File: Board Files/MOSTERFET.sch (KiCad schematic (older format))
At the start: 27 parts, among them CN11 Jumper_NC_Small, CN21 Jumper_NC_Small, J11 XT-60, J12 XT-60, J21 XT-60, J22 XT-60, Q11 AUIRFSA8409-7P, Q21 AUIRFSA8409-7P, U11 TLP182, U21 TLP182

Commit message: Fixed footprint reference
Fixed footprint Reference for open harware symbole
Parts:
- J11, J21: value XT-60 -> XT-60-M; Manufacturer Number XT-60 -> XT-60-M
- J12, J22: value XT-60 -> XT-60-F; Manufacturer Number XT-60 -> XT-60-F
- LO1: footprint MyLib:OPEN_GEAR -> Symbols:OSHW-Symbol_8.9x8mm_SilkScreen
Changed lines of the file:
@@
 P 4925 3750
 F 0 "J12" H 4875 3600 50  0000 L CNN
-F 1 "XT-60" H 5003 3700 50  0001 L CNN
+F 1 "XT-60-F" H 5003 3700 50  0001 L CNN
 F 2 "MyLib:XT60" H 4925 3750 50  0001 C CNN
 F 3 "" H 4925 3750 50  0001 C CNN
-F 4 "XT-60" H 4925 3750 50  0001 C CNN "Manufacturer Number"
+F 4 "XT-60-F" H 4925 3750 50  0001 C CNN "Manufacturer Number"
 F 5 "SparkFun" H 4925 3750 50  0001 C CNN "Supplier"
 F 6 "PRT-10474" H 4925 3750 50  0001 C CNN "Supplier Part No"
@@
 P 4925 3025
 F 0 "J11" H 4875 2875 50  0000 L CNN
-F 1 "XT-60" H 5003 2975 50  0001 L CNN
+F 1 "XT-60-M" H 5003 2975 50  0001 L CNN
 F 2 "MyLib:XT60" H 4925 3025 50  0001 C CNN
 F 3 "" H 4925 3025 50  0001 C CNN
-F 4 "XT-60" H 4925 3025 50  0001 C CNN "Manufacturer Number"
+F 4 "XT-60-M" H 4925 3025 50  0001 C CNN "Manufacturer Number"
 F 5 "SparkFun" H 4925 3025 50  0001 C CNN "Supplier"
 F 6 "PRT-10474" H 4925 3025 50  0001 C CNN "Supplier Part No"
@@
 P 9025 3825
 F 0 "J22" H 8975 3675 50  0000 L CNN
-F 1 "XT-60" H 9103 3775 50  0001 L CNN
+F 1 "XT-60-F" H 9103 3775 50  0001 L CNN
 F 2 "MyLib:XT60" H 9025 3825 50  0001 C CNN
 F 3 "" H 9025 3825 50  0001 C CNN
-F 4 "XT-60" H 9025 3825 50  0001 C CNN "Manufacturer Number"
+F 4 "XT-60-F" H 9025 3825 50  0001 C CNN "Manufacturer Number"
 F 5 "SparkFun" H 9025 3825 50  0001 C CNN "Supplier"
 F 6 "PRT-10474" H 9025 3825 50  0001 C CNN "Supplier Part No"
@@
 P 9025 3100
 F 0 "J21" H 8975 2950 50  0000 L CNN
-F 1 "XT-60" H 9103 3050 50  0001 L CNN
+F 1 "XT-60-M" H 9103 3050 50  0001 L CNN
 F 2 "MyLib:XT60" H 9025 3100 50  0001 C CNN
 F 3 "" H 9025 3100 50  0001 C CNN
-F 4 "XT-60" H 9025 3100 50  0001 C CNN "Manufacturer Number"
+F 4 "XT-60-M" H 9025 3100 50  0001 C CNN "Manufacturer Number"
 F 5 "SparkFun" H 9025 3100 50  0001 C CNN "Supplier"
 F 6 "PRT-10474" H 9025 3100 50  0001 C CNN "Supplier Part No"
@@
 F 0 "LO1" H 1575 7075 50  0001 C CNN
 F 1 "Logo_Open_Hardware_Large" H 1575 6175 50  0001 C CNN
-F 2 "MyLib:OPEN_GEAR" H 1575 6575 50  0001 C CNN
+F 2 "Symbols:OSHW-Symbol_8.9x8mm_SilkScreen" H 1575 6575 50  0001 C CNN
 F 3 "~" H 1575 6575 50  0001 C CNN
 	1    1575 6575

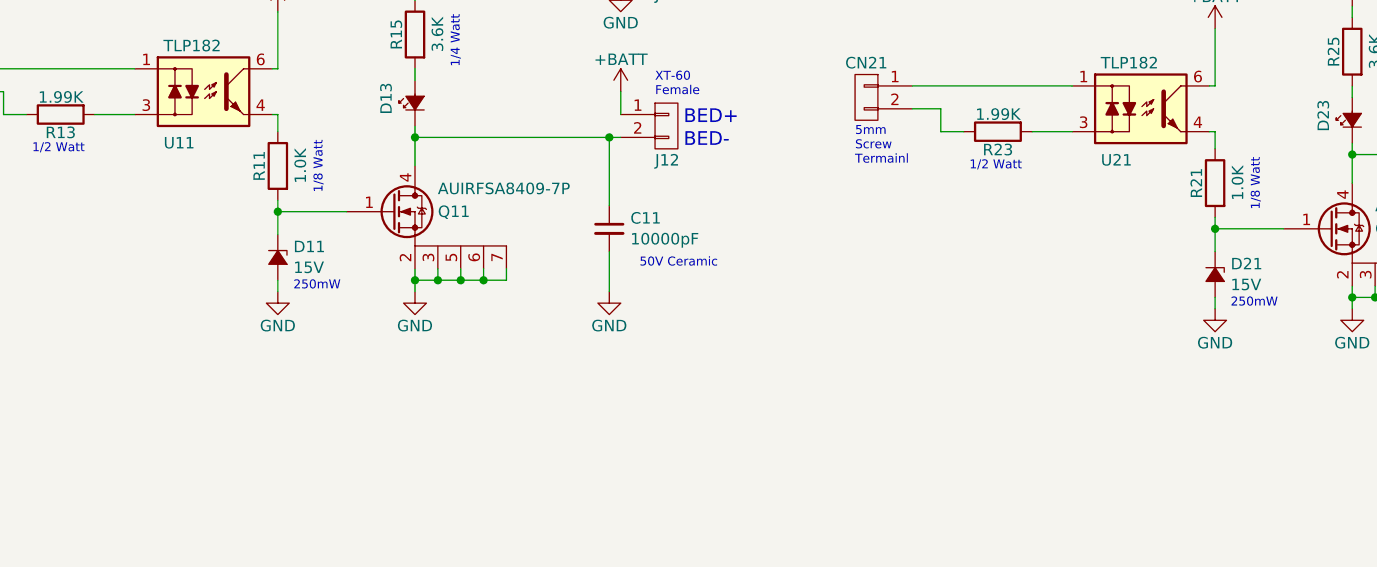
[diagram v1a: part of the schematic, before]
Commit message: Added Bleed resistot
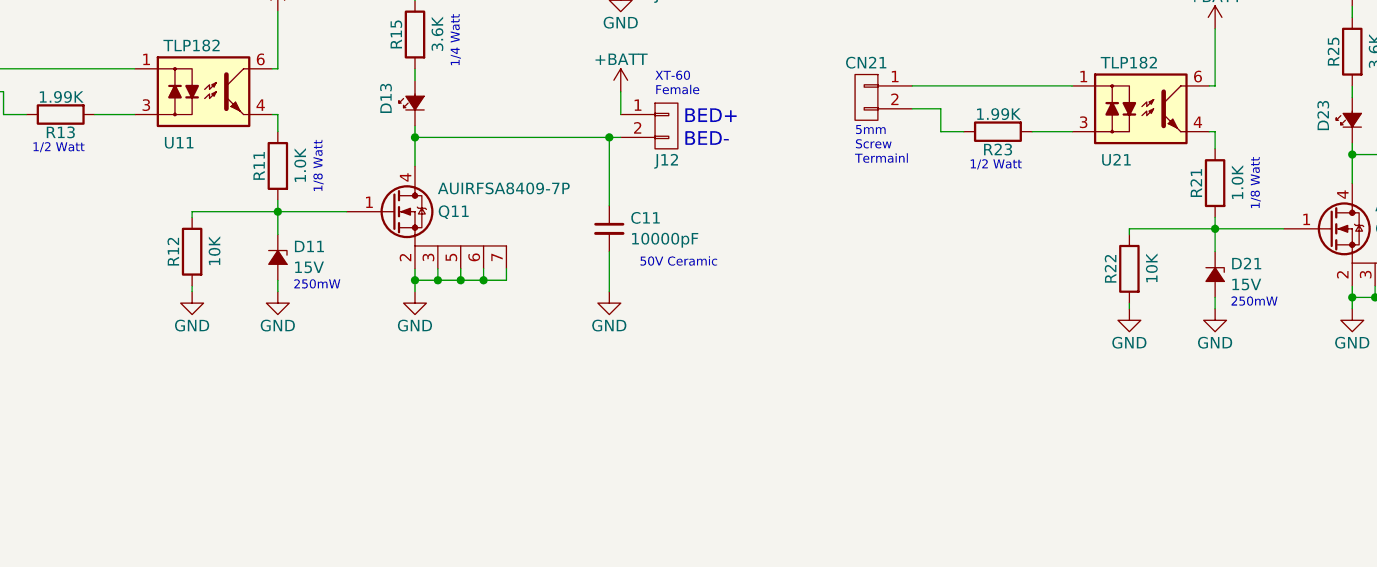
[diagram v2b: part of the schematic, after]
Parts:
- added R12, R22: 10K, Resistors_SMD:R_1206_HandSoldering, symbol Device:R
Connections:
- net GND: now also R12.2, R22.2
- net at D11.3 (K), Q11.1 (G), R11.2: now also R12.1
- net at D21.3 (K), Q21.1 (G), R21.2: now also R22.1
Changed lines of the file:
@@
 Wire Wire Line
 	3825 3800 4675 3800
+$Comp
+L Device:R R12
+U 1 1 5E79AAFD
+P 2850 4300
+F 0 "R12" V 2930 4300 50  0000 C CNN
+F 1 "10K" V 2750 4300 50  0000 C CNN
+F 2 "Resistors_SMD:R_1206_HandSoldering" V 2780 4300 50  0001 C CNN
+F 3 "http://www.yageo.com/NewPortal/yageodocoutput?fileName=/pdf/R-Chip/PYu-RC_Group_51_RoHS_L_4.pdf" H 2850 4300 50  0001 C CNN
+F 4 "RC1206FR-0710KL" H 2850 4300 60  0001 C CNN "Manufacturer Number"
+F 5 "Digi-Key" H 2850 4300 60  0001 C CNN "Supplier"
+F 6 "311-10.0KFRCT-ND" H 2850 4300 60  0001 C CNN "Supplier Part No"
+F 7 "https://www.digikey.com/product-detail/en/yageo/RC1206FR-0710KL/311-10-0KFRCT-ND/731430" H 2850 4300 60  0001 C CNN "Supplier Link"
+F 8 "Yageo" H 2850 4300 60  0001 C CNN "Manufacturer"
+	1    2850 4300
+	-1   0    0    -1
+$EndComp
+$Comp
+L power:GND #PWR?
+U 1 1 5E79BA05
+P 2850 4475
+F 0 "#PWR?" H 2850 4225 50  0001 C CNN
+F 1 "GND" H 2850 4325 50  0000 C CNN
+F 2 "" H 2850 4475 50  0000 C CNN
+F 3 "" H 2850 4475 50  0000 C CNN
+	1    2850 4475
+	-1   0    0    -1
+$EndComp
+Wire Wire Line
+	2850 4475 2850 4450
+Wire Wire Line
+	2850 4150 2850 4125
+Wire Wire Line
+	2850 4125 3225 4125
+$Comp
+L power:GND #PWR?
+U 1 1 5E79F3C5
+P 6950 4550
+F 0 "#PWR?" H 6950 4300 50  0001 C CNN
+F 1 "GND" H 6950 4400 50  0000 C CNN
+F 2 "" H 6950 4550 50  0000 C CNN
+F 3 "" H 6950 4550 50  0000 C CNN
+	1    6950 4550
+	-1   0    0    -1
+$EndComp
+Wire Wire Line
+	6950 4550 6950 4525
+Wire Wire Line
+	6950 4225 6950 4200
+Wire Wire Line
+	6950 4200 7325 4200
+$Comp
+L Device:R R22
+U 1 1 5E7A3262
+P 6950 4375
+F 0 "R22" V 7030 4375 50  0000 C CNN
+F 1 "10K" V 6850 4375 50  0000 C CNN
+F 2 "Resistors_SMD:R_1206_HandSoldering" V 6880 4375 50  0001 C CNN
+F 3 "http://www.yageo.com/NewPortal/yageodocoutput?fileName=/pdf/R-Chip/PYu-RC_Group_51_RoHS_L_4.pdf" H 6950 4375 50  0001 C CNN
+F 4 "RC1206FR-0710KL" H 6950 4375 60  0001 C CNN "Manufacturer Number"
+F 5 "Digi-Key" H 6950 4375 60  0001 C CNN "Supplier"
+F 6 "311-10.0KFRCT-ND" H 6950 4375 60  0001 C CNN "Supplier Part No"
+F 7 "https://www.digikey.com/product-detail/en/yageo/RC1206FR-0710KL/311-10-0KFRCT-ND/731430" H 6950 4375 60  0001 C CNN "Supplier Link"
+F 8 "Yageo" H 6950 4375 60  0001 C CNN "Manufacturer"
+	1    6950 4375
+	-1   0    0    -1
+$EndComp
 $EndSCHEMATC
